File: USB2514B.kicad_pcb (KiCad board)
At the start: 4 copper layers, 70 x 88 mm, 80 parts, among them J1 USB_A, J2 USB_C_Receptacle_USB2.0_16P, J3 USB_A, J4 USB_A, J6 USB_A, U1 USB2514B_Bi, U10 USBLC6-2P6, U11 USBLC6-2P6, U2 USBLC6-2P6, U3 AP22615AWU, U4 MCP1703Ax-330xxTT, U5 AP22615AWU, U6 AP22615AWU, U7 AP22615AWU, U8 USBLC6-2P6, U9 USBLC6-2P6, X1 24MHz

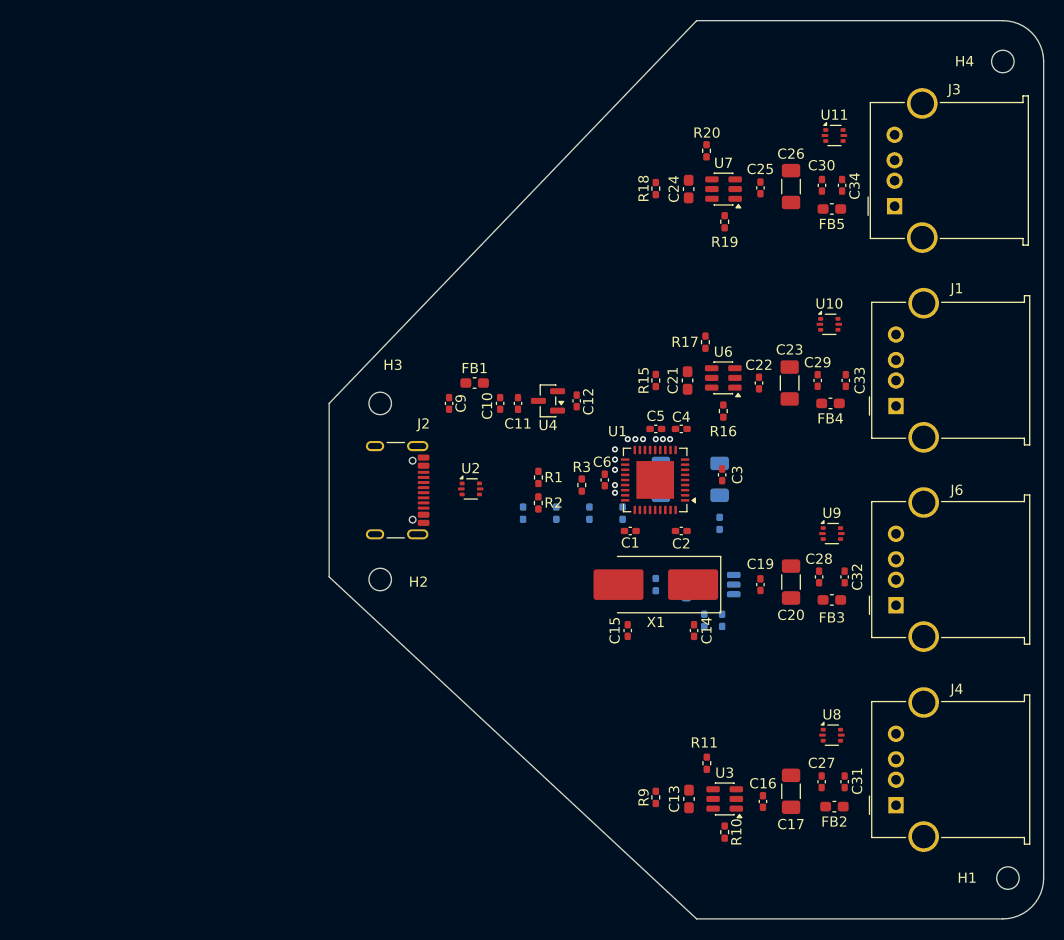
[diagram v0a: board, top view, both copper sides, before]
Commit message: Ajout de toutes les pistes correspondant aux signaux, manque seulement les connexions à l'alimentation et la masse
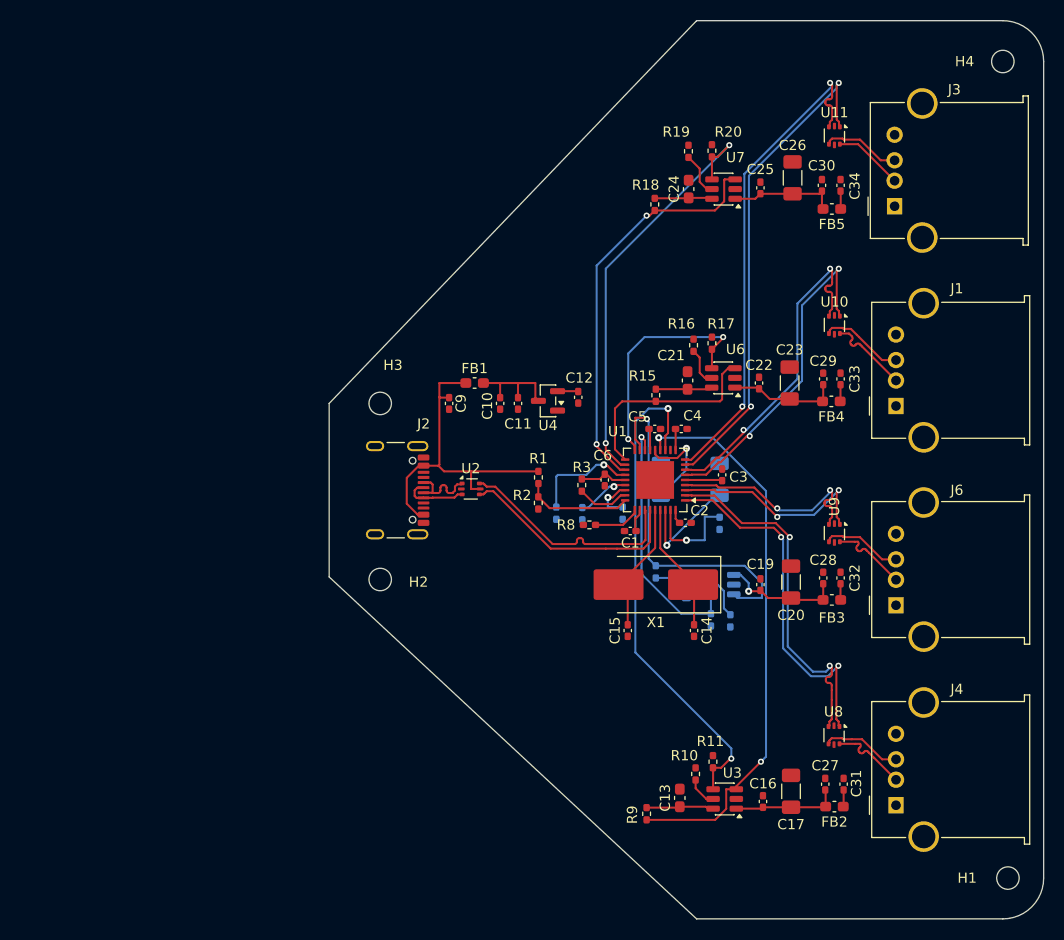
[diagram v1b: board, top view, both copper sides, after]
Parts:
- R8: moved to F.Cu
- moved R19 7.76 mm to (155.2, 78.3), turned to 90 degrees
- moved R16 7.08 mm to (155.7, 97.3), turned to 90 degrees
- moved R8 6.60 mm to (145.5, 114.9), turned to 0 degrees
- moved R10 6.37 mm to (155.9, 139.3), turned to 90 degrees
- moved R9 1.84 mm to (151.1, 143.2), turned to -90 degrees
- moved R18 1.55 mm to (151.9, 83.5), turned to -90 degrees
- moved R15 1.45 mm to (152.0, 102.2), turned to -90 degrees
- moved R12 1.25 mm to (152.0, 119.5), turned to 90 degrees
- moved C13 0.91 mm to (154.3, 141.7)
- moved C2 0.89 mm to (154.9, 114.7)
- moved C26 0.87 mm to (165.4, 80.9)
- moved R13 0.80 mm to (159.3, 124.3), turned to -90 degrees
- moved R5 0.70 mm to (144.8, 113.8)
- moved R14 0.65 mm to (157.4, 124.2)
- moved R17 0.65 mm to (157.5, 97.1)
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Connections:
- net Net-(J1-D+) renamed /D_USB3+
- net Net-(J1-D-) renamed /D_USB3-
- net Net-(J3-D+) renamed /D_USB4+
- net Net-(J3-D-) renamed /D_USB4-
- net Net-(J4-D+) renamed /D_USB1+
- net Net-(J4-D-) renamed /D_USB1-
- net Net-(J6-D+) renamed /D_USB2+
- net Net-(J6-D-) renamed /D_USB2-
- C13 pad 1: /power switches/VIN -> VBUS_FILT
- C18 pad 1: /power switches1/VIN -> VBUS_FILT
- C21 pad 1: /power switches2/VIN -> VBUS_FILT
- C24 pad 1: /power switches3/VIN -> VBUS_FILT
- C32 pad 1: /power switches1/VOUT -> VOUT_PS2
- C33 pad 1: /power switches2/VOUT -> VOUT_PS3
- C34 pad 1: /power switches3/VOUT -> VOUT_PS4
- FB3 pad 2: /power switches1/VOUT -> VOUT_PS2
- FB4 pad 2: /power switches2/VOUT -> VOUT_PS3
- FB5 pad 2: /power switches3/VOUT -> VOUT_PS4
- J1 pad 1: VOUT_PS1 -> VOUT_PS3
- J3 pad 1: VOUT_PS1 -> VOUT_PS4
- J6 pad 1: VOUT_PS1 -> VOUT_PS2
- R11 pad 2: /EN -> /power switches/EN
- R12 pad 1: /power switches1/VIN -> VBUS_FILT
- R14 pad 2: /EN -> /power switches1/EN
- R15 pad 1: /power switches2/VIN -> VBUS_FILT
- R17 pad 2: /EN -> /power switches2/EN
- R18 pad 1: /power switches3/VIN -> VBUS_FILT
- R20 pad 2: /EN -> /power switches3/EN
- R9 pad 1: /power switches/VIN -> VBUS_FILT
- U1 pad 12: /EN -> /power switches/EN
- U1 pad 13: /FAULT -> /power switches/FAULT
- U1 pad 16: /EN -> /power switches1/EN
- U1 pad 17: /FAULT -> /power switches1/FAULT
- U1 pad 18: /EN -> /power switches2/EN
- U1 pad 19: /FAULT -> /power switches2/FAULT
- U1 pad 20: /EN -> /power switches3/EN
- U1 pad 21: /FAULT -> /power switches3/FAULT
- U10 pad 5: VOUT_PS1 -> VOUT_PS3
- U11 pad 5: VOUT_PS1 -> VOUT_PS4
- U3 pad 6: /power switches/VIN -> VBUS_FILT
- U5 pad 6: /power switches1/VIN -> VBUS_FILT
- U6 pad 6: /power switches2/VIN -> VBUS_FILT
- U7 pad 6: /power switches3/VIN -> VBUS_FILT
- U9 pad 5: VOUT_PS1 -> VOUT_PS2
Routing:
- net /power switches/FAULT: track 0.00 -> 55.5 mm, vias 0 -> 2
- net /power switches/EN: track 0.00 -> 49.1 mm, vias 0 -> 2
- net /D_DN4-: track 0.00 -> 48.8 mm, vias 0 -> 2
- net /D_DN4+: track 0.00 -> 48.7 mm, vias 0 -> 2
- net /power switches3/EN: track 0.00 -> 41.7 mm, vias 0 -> 2
- net /power switches3/FAULT: track 0.00 -> 39.8 mm, vias 0 -> 2
- net /D_DN1-: track 0.00 -> 35.1 mm, vias 0 -> 2
- net /D_DN1+: track 0.00 -> 35.1 mm, vias 0 -> 2
- net /power switches1/FAULT: track 0.00 -> 34.7 mm, vias 0 -> 1
- net VBUS_FILT: track 0.00 -> 34.2 mm
- net /D_DN3-: track 0.00 -> 32.8 mm, vias 0 -> 2
- net /D_DN3+: track 0.00 -> 32.7 mm, vias 0 -> 2
- net VBUS: track 0.00 -> 32.6 mm
- net /D_UP-: track 0.00 -> 29.9 mm
- net /D_UP+: track 0.00 -> 29.0 mm
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
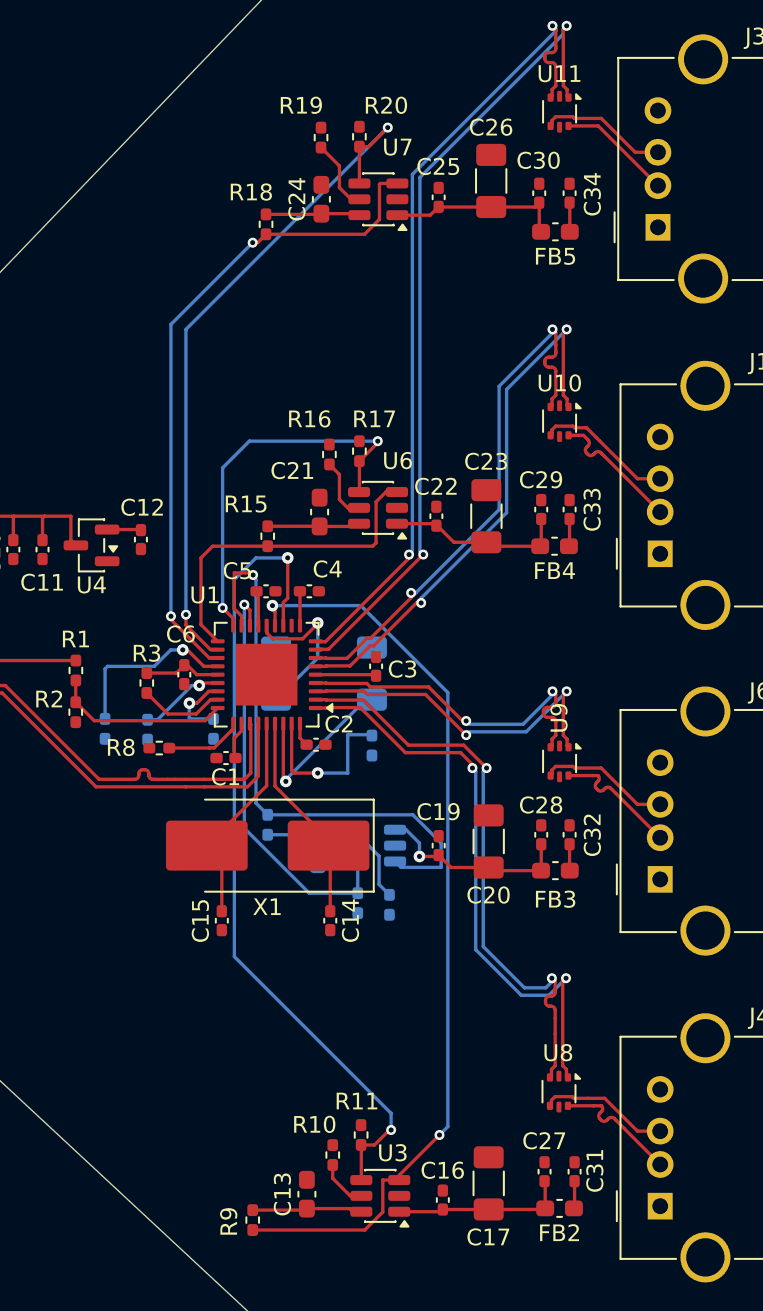
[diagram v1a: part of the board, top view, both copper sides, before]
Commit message: Ajouter pistes alimentation 0.3mm pour 3.3V et 85mA max, connexion à la masse manquant
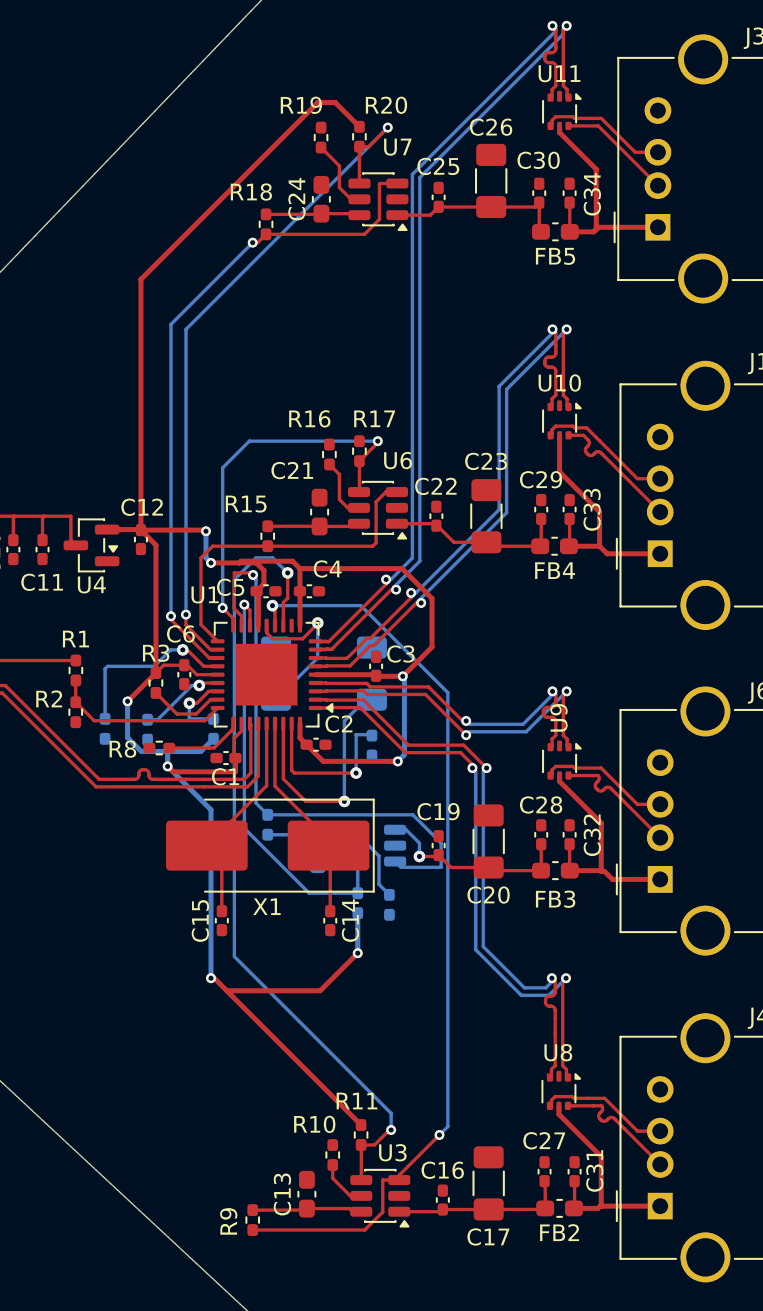
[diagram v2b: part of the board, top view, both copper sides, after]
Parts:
- moved R3 0.55 mm to (145.3, 111.0)
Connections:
- C31 pad 1: /power switches/VOUT -> VOUT_PS1
- FB2 pad 2: /power switches/VOUT -> VOUT_PS1
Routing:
- net +3V3: track 18.3 -> 156.5 mm, vias 0 -> 8
- net VOUT_PS1: track 0.00 -> 13.9 mm
- net VOUT_PS3: track 1.65 -> 14.9 mm
- net VOUT_PS4: track 2.42 -> 15.1 mm
- net VOUT_PS2: track 1.59 -> 13.9 mm
- net Net-(U1-PLLFILT): track 11.5 -> 15.3 mm
- net /power switches/VOUT: track 1.65 -> 0.00 mm
- net /D_DN4-: track 48.8 -> 49.6 mm
- net /D_DN4+: track 48.7 -> 49.6 mm
- net Net-(U1-RESET_N): track 5.13 -> 4.58 mm
- net /power switches/EN: track 49.1 -> 48.6 mm

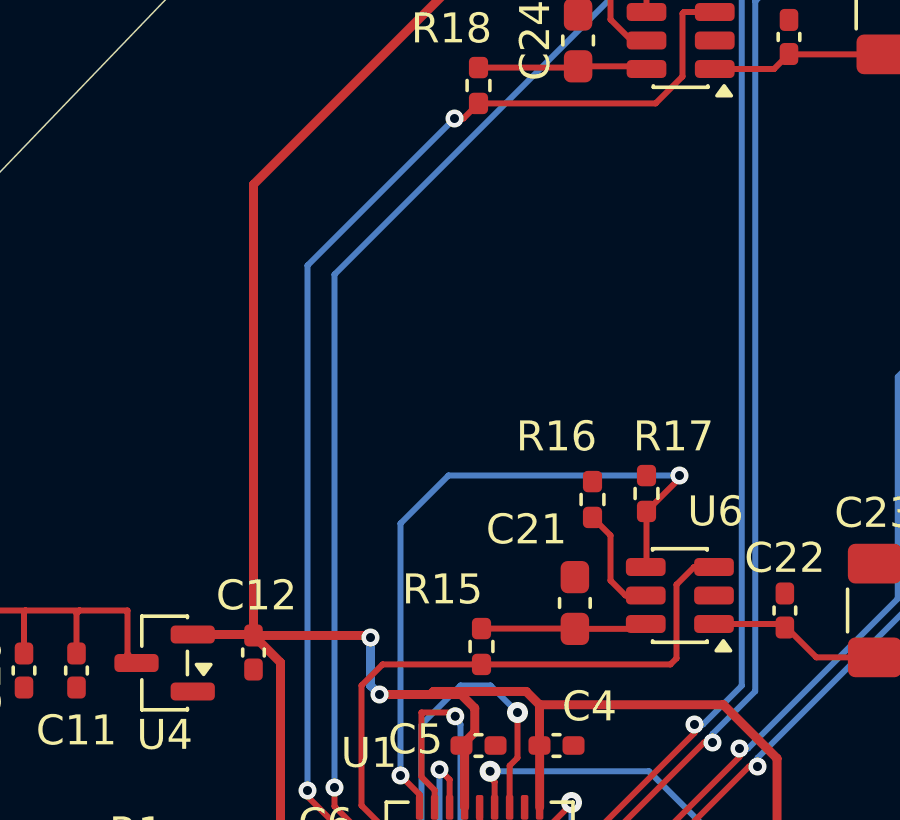
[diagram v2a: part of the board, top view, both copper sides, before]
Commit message: Corrige oublie d'une piste pour alimentation vers J1
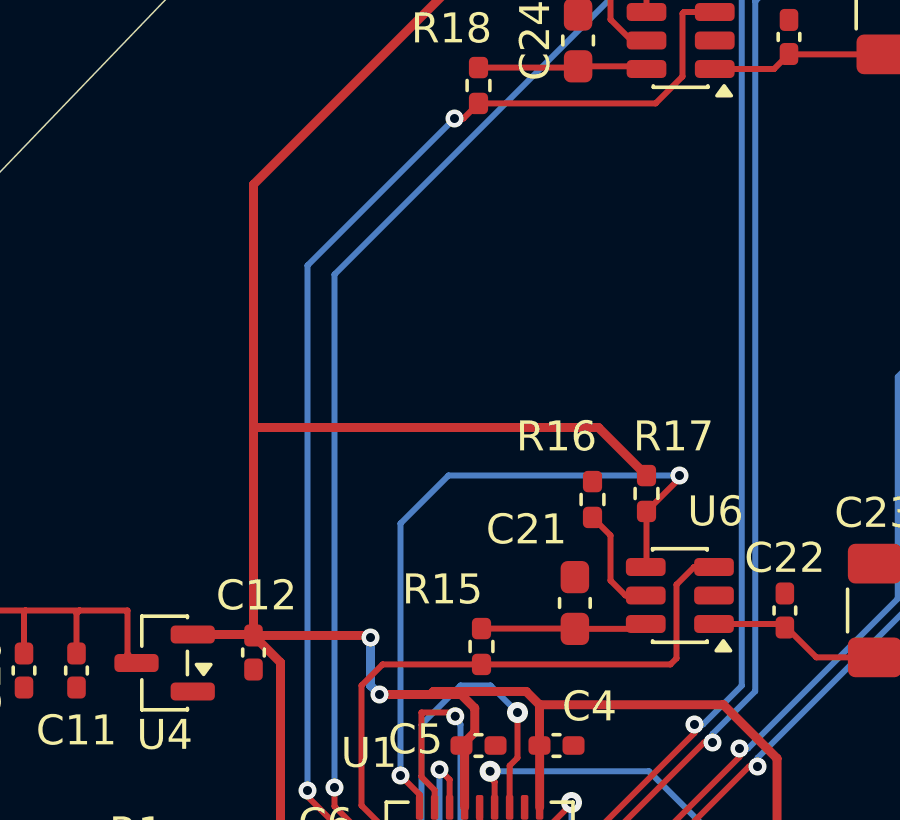
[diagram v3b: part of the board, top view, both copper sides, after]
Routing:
- net +3V3: track 156.5 -> 170.3 mm
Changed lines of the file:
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@@
+	)
+	(segment
+		(start 144.4 94.9)
+		(end 144.4 86.8)
+		(width 0.3)
+		(layer "F.Cu")
+		(net 1)
 	)
 	(segment
@@
 	)
 	(segment
+		(start 144.4 94.9)
+		(end 155.8975 94.9)
+		(width 0.3)
+		(layer "F.Cu")
+		(net 1)
+	)
+	(segment
 		(start 145.3 110.4025)
 		(end 145.2975 110.4025)
@@
 	)
 	(segment
+		(start 155.8975 94.9)
+		(end 157.5 96.5025)
+		(width 0.3)
+		(layer "F.Cu")
+		(net 1)
+	)
+	(segment
 		(start 146.324 116.324)
 		(end 150.0675 116.324)
@@
 	(segment
 		(start 144.4 101.8325)
-		(end 144.4 86.8)
-		(width 0.3)
-		(layer "F.Cu")
+		(end 144.4 94.9)
+		(width 0.3)
+		(layer "F.Cu")

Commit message: Rajoute les connexions oubliées à VBUSFILT
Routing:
- net VBUS_FILT: track 34.2 -> 131.9 mm, vias 0 -> 7
- net /power switches1/EN: track 25.1 -> 27.0 mm
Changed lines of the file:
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@@
 	)
 	(segment
+		(start 147.3 130.5)
+		(end 146.55 129.75)
+		(width 0.2)
+		(layer "F.Cu")
+		(net 6)
+	)
+	(segment
 		(start 136.8 101)
 		(end 138.6 101)
@@
 	)
 	(segment
+		(start 138.9 104.35)
+		(end 138.9 108.9)
+		(width 0.2)
+		(layer "F.Cu")
+		(net 6)
+	)
+	(segment
+		(start 140.2 88.8)
+		(end 140.5 88.5)
+		(width 0.2)
+		(layer "F.Cu")
+		(net 6)
+	)
+	(segment
+		(start 140.5 88.5)
+		(end 146.1 82.9)
+		(width 0.2)
+		(layer "F.Cu")
+		(net 6)
+	)
+	(segment
 		(start 140.200001 102.450001)
 		(end 140.5 102.75)
@@
 	)
 	(segment
+		(start 151.8975 82.9)
+		(end 151.9 82.9025)
+		(width 0.2)
+		(layer "F.Cu")
+		(net 6)
+	)
+	(segment
 		(start 138.5 101.1)
 		(end 138.5 102.4325)
@@
 	)
 	(segment
+		(start 152 124.3)
+		(end 152 122.2)
+		(width 0.2)
+		(layer "F.Cu")
+		(net 6)
+	)
+	(segment
+		(start 147.3 130.5)
+		(end 151.1 134.3)
+		(width 0.2)
+		(layer "F.Cu")
+		(net 6)
+	)
+	(segment
+		(start 150.6 82.9)
+		(end 151.8975 82.9)
+		(width 0.2)
+		(layer "F.Cu")
+		(net 6)
+	)
+	(segment
 		(start 140.2 101)
 		(end 140.200001 102.450001)
@@
 	)
 	(segment
+		(start 140.2 99)
+		(end 142.2 99)
+		(width 0.2)
+		(layer "F.Cu")
+		(net 6)
+	)
+	(segment
 		(start 155.1775 82.9025)
 		(end 155.2195 82.8605)
@@
 	)
 	(segment
+		(start 145.9 129.1)
+		(end 147.3 130.5)
+		(width 0.2)
+		(layer "F.Cu")
+		(net 6)
+	)
+	(segment
+		(start 145.3 99)
+		(end 149.3975 99)
+		(width 0.2)
+		(layer "F.Cu")
+		(net 6)
+	)
+	(segment
+		(start 149.3975 99)
+		(end 152 101.6025)
+		(width 0.2)
+		(layer "F.Cu")
+		(net 6)
+	)
+	(segment
+		(start 151.1 134.3)
+		(end 151.1 142.6025)
+		(width 0.2)
+		(layer "F.Cu")
+		(net 6)
+	)
+	(segment
 		(start 154.26 142.6025)
 		(end 154.35 142.5125)
@@
 	)
 	(segment
+		(start 140.5 102.75)
+		(end 138.9 104.35)
+		(width 0.2)
+		(layer "F.Cu")
+		(net 6)
+	)
+	(segment
 		(start 155.1025 101.6025)
 		(end 155.1125 101.6125)
@@
 	)
 	(segment
+		(start 140.2 99)
+		(end 140.2 88.8)
+		(width 0.2)
+		(layer "F.Cu")
+		(net 6)
+	)
+	(segment
 		(start 138.6 101)
 		(end 140.2 101)
@@
 	)
 	(segment
+		(start 140.2 101)
+		(end 140.2 99)
+		(width 0.2)
+		(layer "F.Cu")
+		(net 6)
+	)
+	(segment
 		(start 155.2195 82.8605)
 		(end 157.4105 82.8605)
@@
 	)
 	(segment
+		(start 146.55 129.75)
+		(end 152 124.3)
+		(width 0.2)
+		(layer "F.Cu")
+		(net 6)
+	)
+	(segment
 		(start 152 101.6025)
 		(end 155.1025 101.6025)
@@
 		(net 6)
 	)
+	(via
+		(at 146.1 82.9)
+		(size 0.6)
+		(drill 0.3)
+		(layers "F.Cu" "B.Cu")
+		(net 6)
+	)
+	(via
+		(at 150.6 82.9)
+		(size 0.6)
+		(drill 0.3)
+		(layers "F.Cu" "B.Cu")
+		(net 6)
+	)
+	(via
+		(at 138.9 108.9)
+		(size 0.6)
+		(drill 0.3)
+		(layers "F.Cu" "B.Cu")
+		(net 6)
+	)
+	(via
+		(at 145.3 99)
+		(size 0.6)
+		(drill 0.3)
+		(layers "F.Cu" "B.Cu")
+		(net 6)
+	)
+	(via
+		(at 145.9 129.1)
+		(size 0.6)
+		(drill 0.3)
+		(layers "F.Cu" "B.Cu")
+		(net 6)
+	)
+	(via
+		(at 142.2 99)
+		(size 0.6)
+		(drill 0.3)
+		(layers "F.Cu" "B.Cu")
+		(net 6)
+	)
+	(via
+		(at 152 122.2)
+		(size 0.6)
+		(drill 0.3)
+		(layers "F.Cu" "B.Cu")
+		(net 6)
+	)
 	(segment
 		(start 154.96 120.0975)
@@
 	)
 	(segment
+		(start 152 122.2)
+		(end 152 120.0975)
+		(width 0.2)
+		(layer "B.Cu")
+		(net 6)
+	)
+	(segment
+		(start 142.2 99)
+		(end 145.3 99)
+		(width 0.2)
+		(layer "B.Cu")
+		(net 6)
+	)
+	(segment
+		(start 145.9 129.1)
+		(end 138.9 122.1)
+		(width 0.2)
+		(layer "B.Cu")
+		(net 6)
+	)
+	(segment
 		(start 155 120.1375)
 		(end 155.8625 120.1375)
@@
 	)
 	(segment
+		(start 138.9 122.1)
+		(end 138.9 108.9)
+		(width 0.2)
+		(layer "B.Cu")
+		(net 6)
+	)
+	(segment
 		(start 152 120.0975)
 		(end 154.96 120.0975)
@@
 	)
 	(segment
+		(start 146.1 82.9)
+		(end 150.6 82.9)
+		(width 0.2)
+		(layer "B.Cu")
+		(net 6)
+	)
+	(segment
 		(start 156.2 119.8)
 		(end 157.3625 119.8)
@@
 	)
 	(segment
-		(start 150.6 106.3)
-		(end 150.6 119.711386)
+		(start 150.6 122.8)
+		(end 151.4025 123.6025)
 		(width 0.2)
 		(layer "B.Cu")
@@
 	)
 	(segment
-		(start 154.491114 123.6025)
+		(start 151.4025 123.6025)
 		(end 157.4 123.6025)
 		(width 0.2)
@@
 	)
 	(segment
-		(start 150.6 119.711386)
-		(end 154.491114 123.6025)
+		(start 150.6 106.3)
+		(end 150.6 122.8)
 		(width 0.2)
 		(layer "B.Cu")
